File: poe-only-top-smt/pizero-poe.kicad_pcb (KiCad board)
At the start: 2 copper layers, 81.8 x 30 mm, 80 parts, among them IC1 ENC28J60-I/ML, J1 RJ45-LED, P2 dnp-REF-182665-01, Q1 SI3440DV, Q2 DMMT3906_Dual_PNP, Q3 Q_PMOS_GSD, T1 PULSE_H1197, T2 TRANSFO, T3 VOLTAGE_REF, U1 LTC4267, U2 PAS291, U3 dnp-AT24CS32-SSHM, U4 AP7365_SOT-23-5, Y1 25Mhz

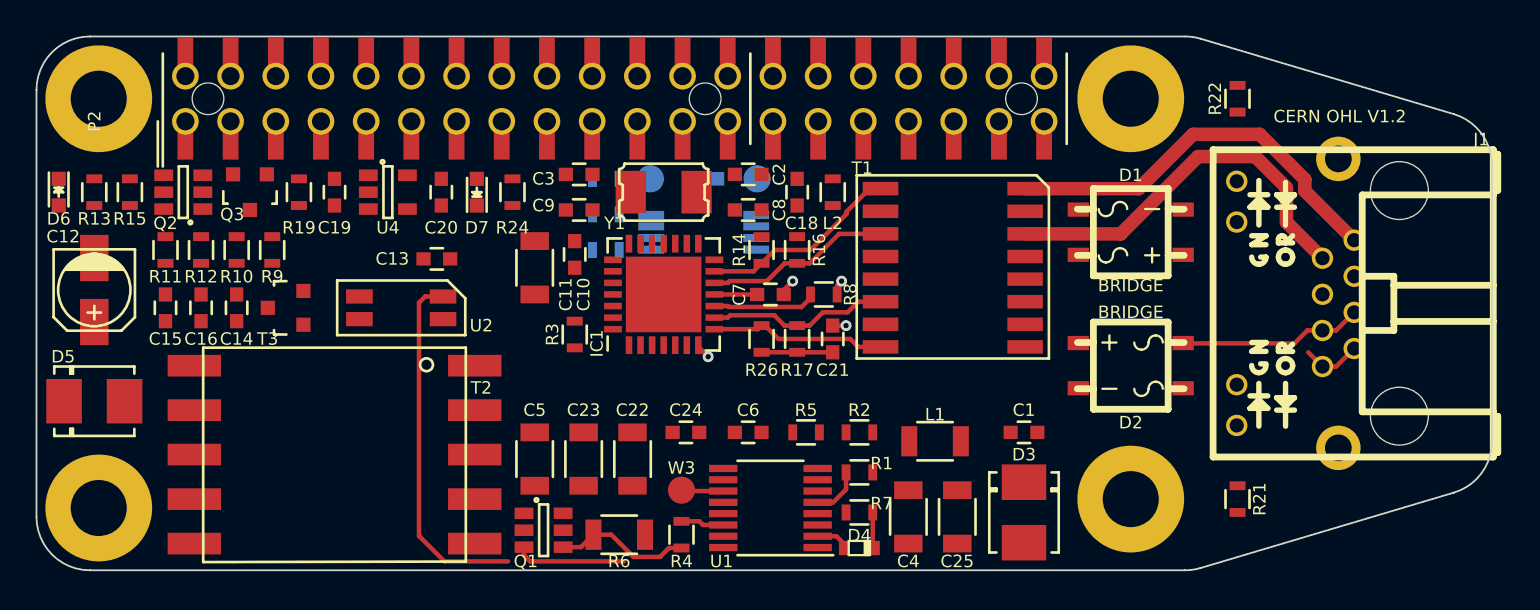
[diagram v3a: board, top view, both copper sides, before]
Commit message: complete routing for poe and ethernet
* isolate to ~500Vac with .75-.8mm gaps between high and low voltage copper
* remove extra 2x13 compatibility holes from pizero_poe_special:Pin_Header_Straight_TH-SMT-NoPaste_2x20, Pin_Header_Straight_TH-SMT_2x20 footprints
* add insert attribute to pizero_poe_special:Crystal_Grounded_3.2x2.5, MBS, Pin_Header_Straight_TH-SMT_2x20, sod123, sod323, sod523 footprints.
* change rpi hat eeprom power from RPI_3V3_2 to +3V3
* calculate trace geometry for ethenet impedance control
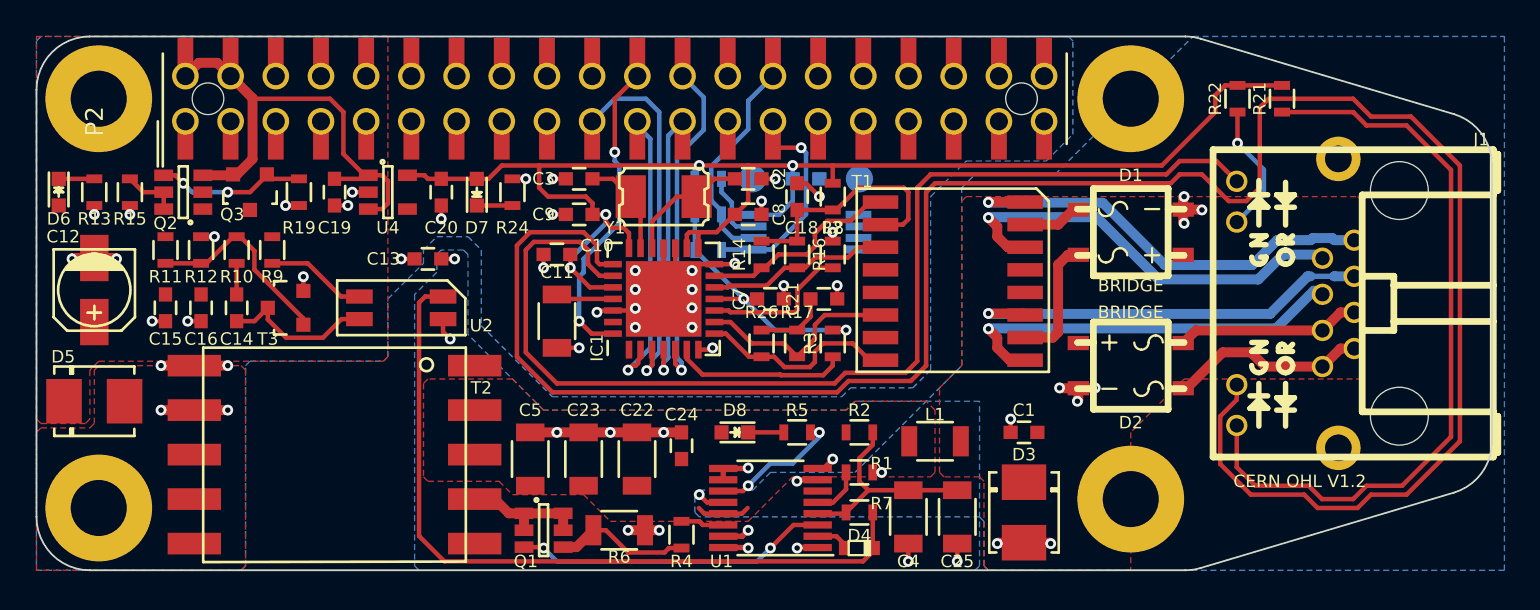
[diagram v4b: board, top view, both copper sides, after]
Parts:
- removed C6: DNP, Capacitors_SMD:C_0603
- removed W3: TEST_1P, Measurement_Points:Measurement_Point_Round-SMD-Pad_Small
- added D8: LED Green, LEDs:LED_0603, F.Cu at (145.3, 100.0)
- R5: value DNP -> 23k
- moved R21 22.6 mm to (176.1, 81.2), turned to 90 degrees
- moved R3 14.5 mm to (150.8, 95.0)
- moved C17 5.75 mm to (149.3, 85.7)
- moved R18 5.75 mm to (143.8, 85.7)
- moved R20 5.75 mm to (143.8, 89.7)
- moved R23 5.75 mm to (143.8, 87.7)
- moved U3 5.75 mm to (149.3, 88.7)
- moved W1 5.75 mm to (152.3, 85.7)
- moved W2 5.75 mm to (146.3, 85.7)
- moved C11 3.25 mm to (135.3, 93.7), turned to 90 degrees
- moved C21 2.30 mm to (150.3, 92.5), turned to 0 degrees
- moved R8 2.30 mm to (150.8, 90.0), turned to 270 degrees
- moved C10 1.00 mm to (135.3, 90.0), turned to 180 degrees
- moved C24 0.79 mm to (142.3, 100.7), turned to 90 degrees
- moved T1 0.75 mm to (157.6, 91.5)
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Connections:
- C17 pad 1: /RPI_3V3_2 -> +3V3
- IC1 pad 28: /GPIO_25 -> /GPIO25
- R18 pad 1: /RPI_3V3_2 -> +3V3
- R20 pad 1: /RPI_3V3_2 -> +3V3
- R23 pad 1: /RPI_3V3_2 -> +3V3
- R5 pad 1: /POE_SW_D -> Net-(D8-Pad1)
- R5 pad 2: Net-(C6-Pad2) -> /~POE_PWRGD
- U3 pad 8: /RPI_3V3_2 -> +3V3
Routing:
- net /LEDB_K: track 0.00 -> 121.4 mm
- net +3V3: track 2.40 -> 100.3 mm, vias 0 -> 6
- net /LEDA_K: track 0.00 -> 64.1 mm
- net GND: track 3.44 -> 62.3 mm, vias 4 -> 39
- net /LEDB_A: track 0.00 -> 42.4 mm
- net /RPI_VBUS: track 0.00 -> 29.5 mm
- net /TPIN_T+: track 0.00 -> 23.5 mm, vias 0 -> 1
- net /TPIN_T-: track 0.00 -> 22.9 mm, vias 0 -> 1
- net /GPIO10_MOSI: track 0.00 -> 22.0 mm, vias 0 -> 1
- net GNDPWR: track 0.00 -> 21.5 mm, vias 0 -> 14
- net /POE_RUN: track 22.2 -> 43.2 mm
- net /GPIO8_CE0#: track 0.00 -> 20.3 mm, vias 0 -> 1
- net /GPIO25: track 0.00 -> 18.8 mm, vias 0 -> 2
- net /GPIO9_MISO: track 0.00 -> 17.7 mm, vias 0 -> 1
- net /GPIO11_SCLK: track 0.00 -> 16.9 mm, vias 0 -> 1
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- added copper zone on F.Cu, net +5V
- added copper zone on B.Cu, net /POE_VPORTN
- added copper zone on F.Cu, net /POE_VPORTP
- added copper zone on F.Cu, net /POE_VPORTP_L
- added copper zone on B.Cu, net GND
- added copper zone on B.Cu, net GNDPWR
- added copper zone on F.Cu, net Net-(D5-Pad2)
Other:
- net class PoE Power: trace_width 0.762 -> 0.5588

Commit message: add datasheets, change eth magnetics, clean up silkscreen
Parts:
- T1: value PULSE_H1197 -> H2019FNL; footprint project_foot:H2019 -> pizero-poe-special:Transformer_Pulse_H2019FNL
- turned T1 to 0 degrees
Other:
- board text added: "3V3"
- board text added: "5V"
- board text added: "PoE PG"
- board text added: "RPi 0 PoE Rev 1.0 CERN OHL V1.2 ihartwig '16"
- board text added: "RPi 0 PoE Rev 1.0 ihartwig '16"
- board text removed: "CERN OHL V1.2"

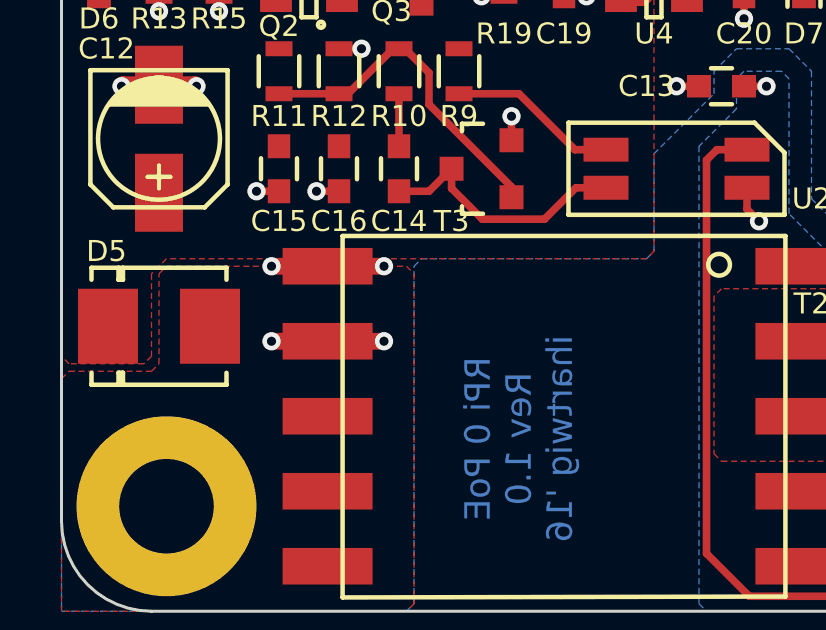
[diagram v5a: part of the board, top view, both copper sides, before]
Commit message: add part info to schematic for BOM. TODO: UPDATE LAYOUT
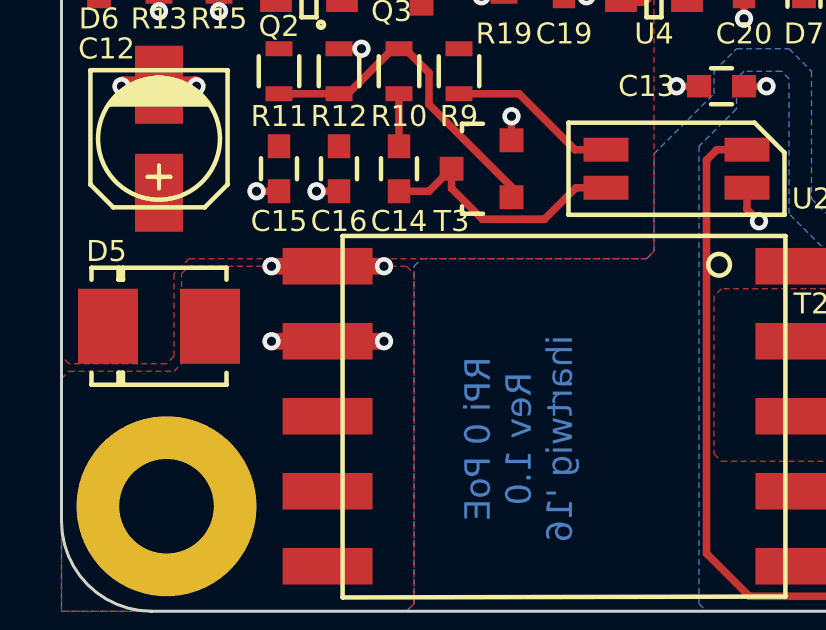
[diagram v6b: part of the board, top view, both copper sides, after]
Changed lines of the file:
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@@
 (kicad_pcb (version 4) (host pcbnew 4.0.2-stable)
   (general
-    (links 244)
+    (links 0)
     (no_connects 0)
-    (area 106.049999 77.649999 187.950001 107.750001)
+    (area 98.244948 73.736238 188.672501 113.300001)
     (thickness 1.6)
     (drawings 19)
@@
     (visible_elements 7FFFFF7F)
     (pcbplotparams
-      (layerselection 0x010f0_80000001)
-      (usegerberextensions false)
+      (layerselection 0x010fc_80000001)
+      (usegerberextensions true)
       (excludeedgelayer true)
       (linewidth 0.100000)
@@
       (viasonmask false)
       (mode 1)
-      (useauxorigin false)
+      (useauxorigin true)
       (hpglpennumber 1)
       (hpglpenspeed 20)
@@
       (drillshape 0)
       (scaleselection 1)
-      (outputdirectory /home/mangokid/Desktop/hat_gerber/))
+      (outputdirectory gerber/))
   )
   (net 0 "")
@@
   (module project_foot:PoE_TRANS (layer F.Cu)
     (at 122.85 101.2 90)
+    (attr smd)
     (fp_text reference T2 (at 3.75 8.25 180) (layer F.SilkS)
       (effects (font (size 0.7 0.7) (thickness 0.15)))
@@
     (at 141.35 86.7 180)
     (descr "5x3.2mm SMD glass Crystal")
+    (attr smd)
     (fp_text reference Y1 (at 2.75 -1.75 180) (layer F.SilkS)
       (effects (font (size 0.7 0.7) (thickness 0.15)))
@@
   (module project_foot:OPTO_ISO (layer F.Cu)
     (at 126.6 92.95 270)
+    (attr smd)
     (fp_text reference U2 (at 1 -4.5 360) (layer F.SilkS)
       (effects (font (size 0.7 0.7) (thickness 0.15)))
@@
   (module pizero-poe-special:MBS (layer F.Cu)
     (at 167.6 88.7)
+    (attr smd)
     (fp_text reference D1 (at 0 -3.2004) (layer F.SilkS)
       (effects (font (size 0.7 0.7) (thickness 0.15)))
@@
   (module pizero-poe-special:MBS (layer F.Cu)
     (at 167.6 96.2 180)
+    (attr smd)
     (fp_text reference D2 (at 0 -3.2004 180) (layer F.SilkS)
       (effects (font (size 0.7 0.7) (thickness 0.15)))
@@
     (at 152.35 106.45)
     (descr SOD523)
+    (attr smd)
     (fp_text reference D4 (at 0 -0.70104) (layer F.SilkS)
       (effects (font (size 0.7 0.7) (thickness 0.15)))
@@
   (module pizero-poe-special:Transformer_Pulse_H2019FNL (layer F.Cu)
     (at 157.6 91.45)
+    (attr smd)
     (fp_text reference T1 (at 5.25 -6) (layer F.SilkS)
       (effects (font (size 0.7 0.7) (thickness 0.15)))
@@
       (pts
         (xy 117.85 107.45) (xy 117.6 107.7) (xy 106.1 107.7) (xy 106.1 99.95) (xy 106.35 99.7)
-        (xy 109.1 99.7) (xy 109.35 99.45) (xy 109.35 96.45) (xy 109.6 96.2) (xy 117.6 96.2)
+        (xy 109.85 99.7) (xy 110.1 99.45) (xy 110.1 96.45) (xy 110.35 96.2) (xy 117.6 96.2)
         (xy 117.85 96.45)
       )
@@
   )
   (zone (net 5) (net_name +5V) (layer F.Cu) (hatch edge 0.508)
+    (priority 1)
     (connect_pads (clearance 0.2032))
     (min_thickness 0.254)
@@
       (pts
         (xy 106.1 96.95) (xy 106.1 95.7) (xy 106.1 77.7) (xy 125.85 77.7) (xy 125.85 95.7)
-        (xy 125.6 95.95) (xy 109.6 95.95) (xy 109.1 96.45) (xy 109.1 99.2) (xy 108.85 99.45)
+        (xy 125.6 95.95) (xy 110.35 95.95) (xy 109.85 96.45) (xy 109.85 99.2) (xy 109.6 99.45)
         (xy 106.35 99.45) (xy 106.1 99.2)
       )

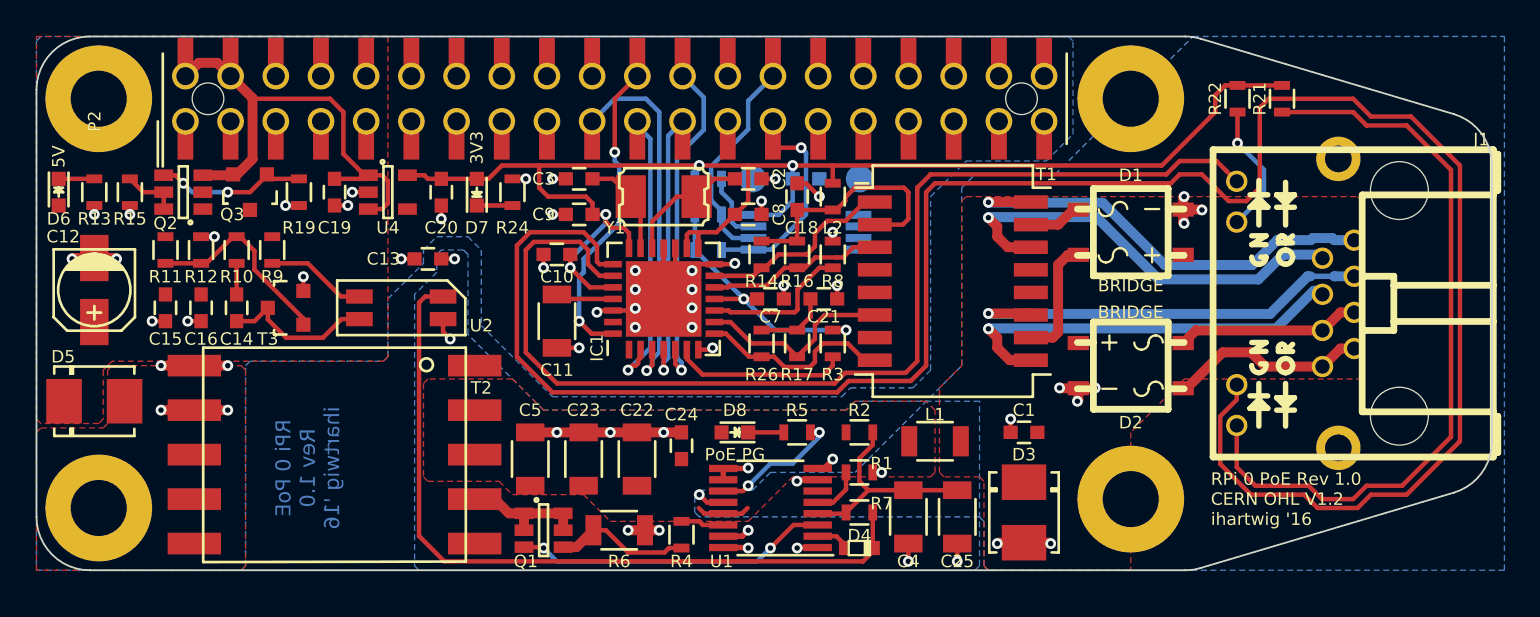
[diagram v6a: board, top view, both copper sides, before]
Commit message: fix layout for larger cap, isolation, solder mask
* larger footprint for 470uF cap and adjust power and phy to fit
* fix 3d model of rpi header for 20 pins
* add soldermask expansion
* allow soldermask tenting on ethernet phy ep
* add gerbers
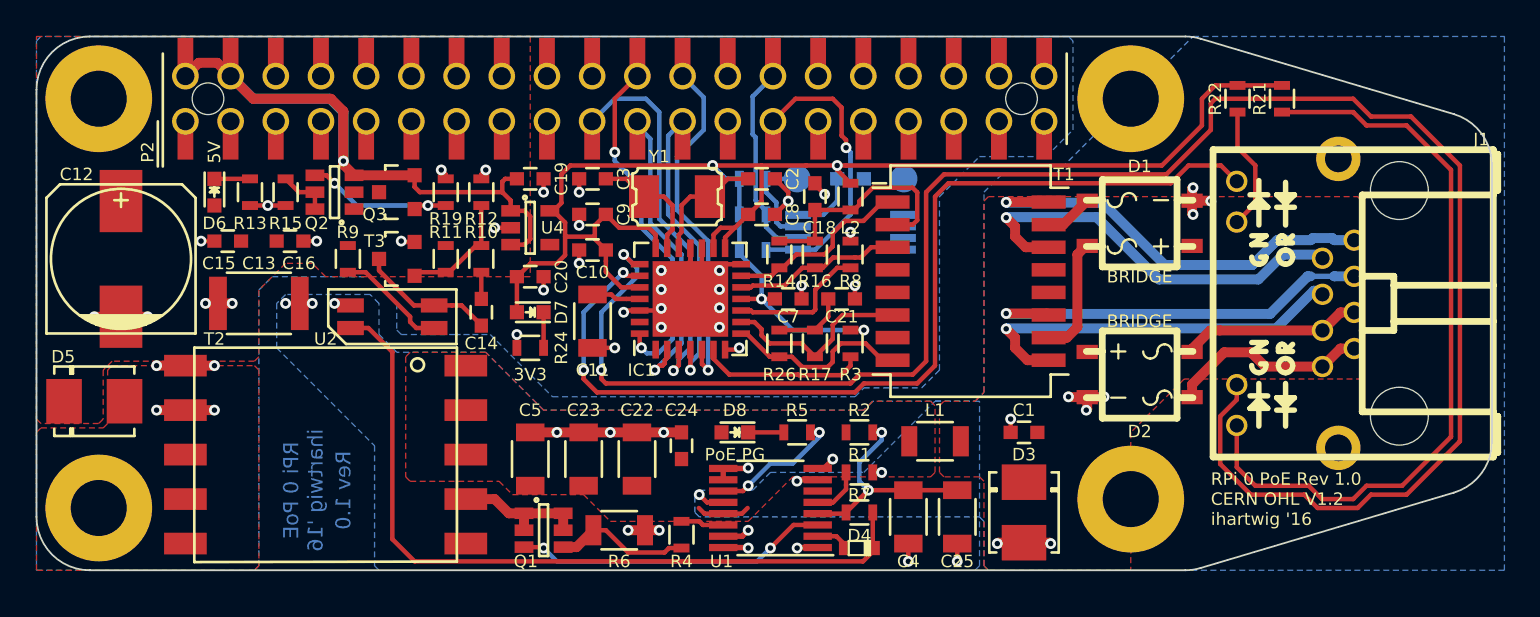
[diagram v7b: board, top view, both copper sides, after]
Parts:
- C12: footprint Capacitors_SMD:c_elec_4x4.5 -> Capacitors_SMD:c_elec_8x10
- C13: value 2nf -> 2.2nF 250Vac; footprint Capacitors_SMD:C_0603 -> Capacitors_SMD:C_1812
- C17: value dnp-100n -> nostuff-0.1u
- R1: value DNP -> nostuff
- R18: value dnp-1k -> nostuff-1k
- R20, R23: value dnp-3.9k -> nostuff-3.9k
- U2: value PAS291 -> PS2911-1-K-AX
- U3: value dnp-AT24CS32-SSHM -> nostuff-AT24CS32-SSHM
- moved R12 16.1 mm to (131.1, 86.5)
- moved R11 15.8 mm to (129.1, 90.2)
- moved R10 13.8 mm to (131.1, 90.2)
- moved C14 13.8 mm to (131.1, 93.2)
- moved C19 11.0 mm to (133.8, 85.7), turned to 0 degrees
- moved C13 9.82 mm to (118.6, 92.7)
- moved R24 8.81 mm to (133.8, 95.2), turned to 180 degrees
- moved D6 8.75 mm to (116.1, 86.5)
- moved R13 8.75 mm to (118.1, 86.5)
- moved R15 8.75 mm to (120.1, 86.5)
- moved Q2 8.50 mm to (122.8, 86.5)
- moved Q3 8.25 mm to (126.3, 86.5), turned to 90 degrees
- moved R19 8.25 mm to (129.1, 86.5), turned to 90 degrees
- moved U4 8.25 mm to (133.8, 88.5)
- moved D7 7.39 mm to (133.8, 93.2), turned to 180 degrees
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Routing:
- net /LEDB_K: track 121.4 -> 108.6 mm, vias 0 -> 2
- net /RPI_VBUS: track 29.5 -> 42.3 mm, vias 0 -> 1
- net /LEDA_K: track 64.1 -> 56.1 mm, vias 0 -> 2
- net /GPIO0_ID_SD: track 12.4 -> 17.7 mm
- net /POE_FB_DIV: track 11.2 -> 6.70 mm
- net +3V3: track 100.3 -> 97.2 mm, vias 6 -> 4
- net /GPIO25: track 18.8 -> 21.0 mm
- net /PHY_OSC2: track 5.69 -> 6.90 mm
- net /POE_FB_K: track 8.72 -> 7.70 mm
- net /TPOUT_T-: track 24.3 -> 23.3 mm
- net /TPOUT_T+: track 25.1 -> 24.1 mm
- net /TPIN_T-: track 23.2 -> 22.2 mm
- net /TPIN_T+: track 23.9 -> 22.9 mm
- net Net-(C18-Pad2): track 13.9 -> 13.0 mm
- net /GPIO1_ID_SC: track 13.5 -> 12.6 mm
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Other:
- rule pad_to_mask_clearance: 0 -> 0.051
- board text added: "RPi 0 PoE ihartwig '16"
- board text added: "Rev 1.0"
- board text removed: "RPi 0 PoE Rev 1.0 ihartwig '16"
